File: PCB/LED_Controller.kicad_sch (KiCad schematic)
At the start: 44 parts, among them J1 Conn_01x04_Female, J2 Conn_01x06_Female, J3 Conn_01x06_Female, J4 Add. LED Strip, J5 Add. LED Strip, J7 Conn_01x02, Q1 MMBF170, Q10 BC817, Q2 MMBF170, Q3 MMBF170, Q4 MMBF170, Q9 BC817, SW1 SW_Push, SW2 SW_Push, U1 ESP32-WROOM-32, U2 NCP1117-5.0_SOT223, U3 NCP1117-3.3_SOT223

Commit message: Rev 2.0 local push
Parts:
- removed J1: Conn_01x04_Female, Connector_PinHeader_2.54mm:PinHeader_2x02_P2.54mm_Vertical, symbol Connector:Conn_01x04_Female
- removed J3: Conn_01x06_Female, Connector_PinHeader_2.54mm:PinHeader_2x03_P2.54mm_Vertical, symbol Connector:Conn_01x06_Female
- removed J5: Add. LED Strip, TerminalBlock_Phoenix:TerminalBlock_Phoenix_MKDS-1,5-4-5.08_1x04_P5.08mm_Horizontal, symbol Connector_Generic:Conn_01x04
- removed JP3: Jumper_2_Bridged, Jumper:SolderJumper-2_P1.3mm_Bridged2Bar_Pad1.0x1.5mm, symbol Jumper:Jumper_2_Bridged
- removed JP4: Jumper_3_Bridged12, Jumper:SolderJumper-3_P1.3mm_Bridged2Bar12_Pad1.0x1.5mm, symbol Jumper:Jumper_3_Bridged12
- removed Q1, Q2, Q3, Q4: MMBF170, Package_TO_SOT_SMD:SOT-23, symbol Transistor_FET:MMBF170
- removed Q10, Q9: BC817, Package_TO_SOT_SMD:SOT-23, symbol Transistor_BJT:BC817
- removed R10, R11, R12, R13, R19, R20, R5, R6, R8, R9: 10k, Resistor_SMD:R_0805_2012Metric_Pad1.20x1.40mm_HandSolder, symbol Device:R
- removed SW1, SW2: SW_Push, Button_Switch_SMD:SW_Push_1P1T_NO_CK_KMR2, symbol Switch:SW_Push
- removed U1: ESP32-WROOM-32, RF_Module:ESP32-WROOM-32, symbol RF_Module:ESP32-WROOM-32
- removed U2: NCP1117-5.0_SOT223, Package_TO_SOT_SMD:SOT-223-3_TabPin2, symbol Regulator_Linear:NCP1117-5.0_SOT223
- removed U3: NCP1117-3.3_SOT223, Package_TO_SOT_SMD:SOT-223-3_TabPin2, symbol Regulator_Linear:NCP1117-3.3_SOT223
- added AE1: Antenna_Chip, RF_Antenna:Johanson_2450AT43F0100, symbol Device:Antenna_Chip
- added C10, C11: C, Capacitor_SMD:C_0805_2012Metric_Pad1.18x1.45mm_HandSolder, symbol Device:C
- added C9: 0.1u, Capacitor_SMD:C_0603_1608Metric, symbol Device:C_Small
- added J1: Barrel_Jack, Connector_BarrelJack:BarrelJack_Horizontal, symbol Connector:Barrel_Jack
- added JP1: Jumper_2_Bridged, Jumper:SolderJumper-2_P1.3mm_Bridged2Bar_Pad1.0x1.5mm, symbol Jumper:Jumper_2_Bridged
- added L1: 3.3uH, Inductor_SMD:L_1206_3216Metric_Pad1.22x1.90mm_HandSolder, symbol Device:L
- added L2: L, Inductor_SMD:L_0805_2012Metric_Pad1.05x1.20mm_HandSolder, symbol Device:L
- added U1: ESP32-PICO-D4, Package_DFN_QFN:QFN-48-1EP_7x7mm_P0.5mm_EP5.3x5.3mm, symbol RF_Module:ESP32-PICO-D4
- added U2: AP62200, Package_TO_SOT_SMD:SOT-563, symbol Regulator_Switching:AP62250Z6
- added U3: NCP1117-5.0_SOT223, Package_TO_SOT_SMD:SOT-223-3_TabPin2, symbol Regulator_Linear:NCP1117-5.0_SOT223
- added U4: 74LVCH2T45DC, Package_SO:VSSOP-8_2.3x2mm_P0.5mm, symbol Logic_LevelTranslator:74LVCH2T45DC
- C1: value 10uF -> 0.1uF
- C2: value 0.1uF -> 22uF; footprint Capacitor_SMD:C_0805_2012Metric_Pad1.18x1.45mm_HandSolder -> Capacitor_SMD:C_1206_3216Metric_Pad1.33x1.80mm_HandSolder
- C5: footprint Capacitor_SMD:C_0805_2012Metric_Pad1.18x1.45mm_HandSolder -> Capacitor_SMD:C_1206_3216Metric_Pad1.33x1.80mm_HandSolder
- R4: value 10k -> 31.6k
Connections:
- net PROG_DTR is gone; now on net EN: J2.4 (Pin_4)
- net PROG_RTS is gone; now on net GPIO0: J2.5 (Pin_5)
- net VLED is gone; now on net VIN: C7.1, C8.1, J4.4 (Pin_4)
- net +3V3: now also C2.1, R4.2, C9.1, L1.2, U1.1 (VDDA), U1.19 (VDD3P3_RTC), U1.26 (VDD_SDIO), U1.3 (VDDA3P3), U1.37 (VDD3P3_CPU), U1.4 (VDDA3P3), U1.43 (VDDA), U1.46 (VDDA), U4.1 (VCCA), U4.5 (DIR); no longer R1.1
- net +5V: now also JP1.2 (B), U3.2 (VO), U4.8 (VCCB); no longer C1.1, C2.1, R4.1
- net EN: now also U1.9 (EN)
- net GND: now also R1.1, C10.2, C11.2, C9.2, J1.2, U1.49 (GND), U2.3 (GND), U3.1 (GND), U4.4 (GND); no longer C1.2
- net GPIO0: now also U1.23 (IO0)
- net LED1-CLK_{H}: now also U4.6 (2B)
- net LED1-CLK_{L}: now also U1.16 (IO27), U4.3 (2A)
- net LED1-DATA_{H}: now also U4.7 (1B); no longer R4.2
- net LED1-DATA_{L}: now also U1.17 (IO14), U4.2 (1A); no longer R1.2
- net MIC_SCK: now also U1.13 (IO33)
- net MIC_SD: now also U1.11 (IO35)
- net MIC_WS: now also U1.10 (IO34)
- net RX: now also U1.40 (U0RXD/IO3)
- net TX: now also R7.1, U1.41 (U0TXD/IO1); no longer J2.2 (Pin_2), R7.2
- net VIN: now also J1.1, JP1.1 (A), U2.1 (VIN), U2.5 (EN), U3.3 (VI)
- new net: C1.2, L1.1, U2.2 (SW)
- new net: AE1.1 (FEED), C11.1, L2.2
- new net: J2.2 (Pin_2), R7.2
- new net: R1.2, R4.1, U2.6 (FB)
- new net: C10.1, L2.1, U1.2 (LNA_IN)
- new net: C1.1, U2.4 (BST)
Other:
- moved on the sheet: C3, C4, C5, C6, C7, C8, J2, J7, R7

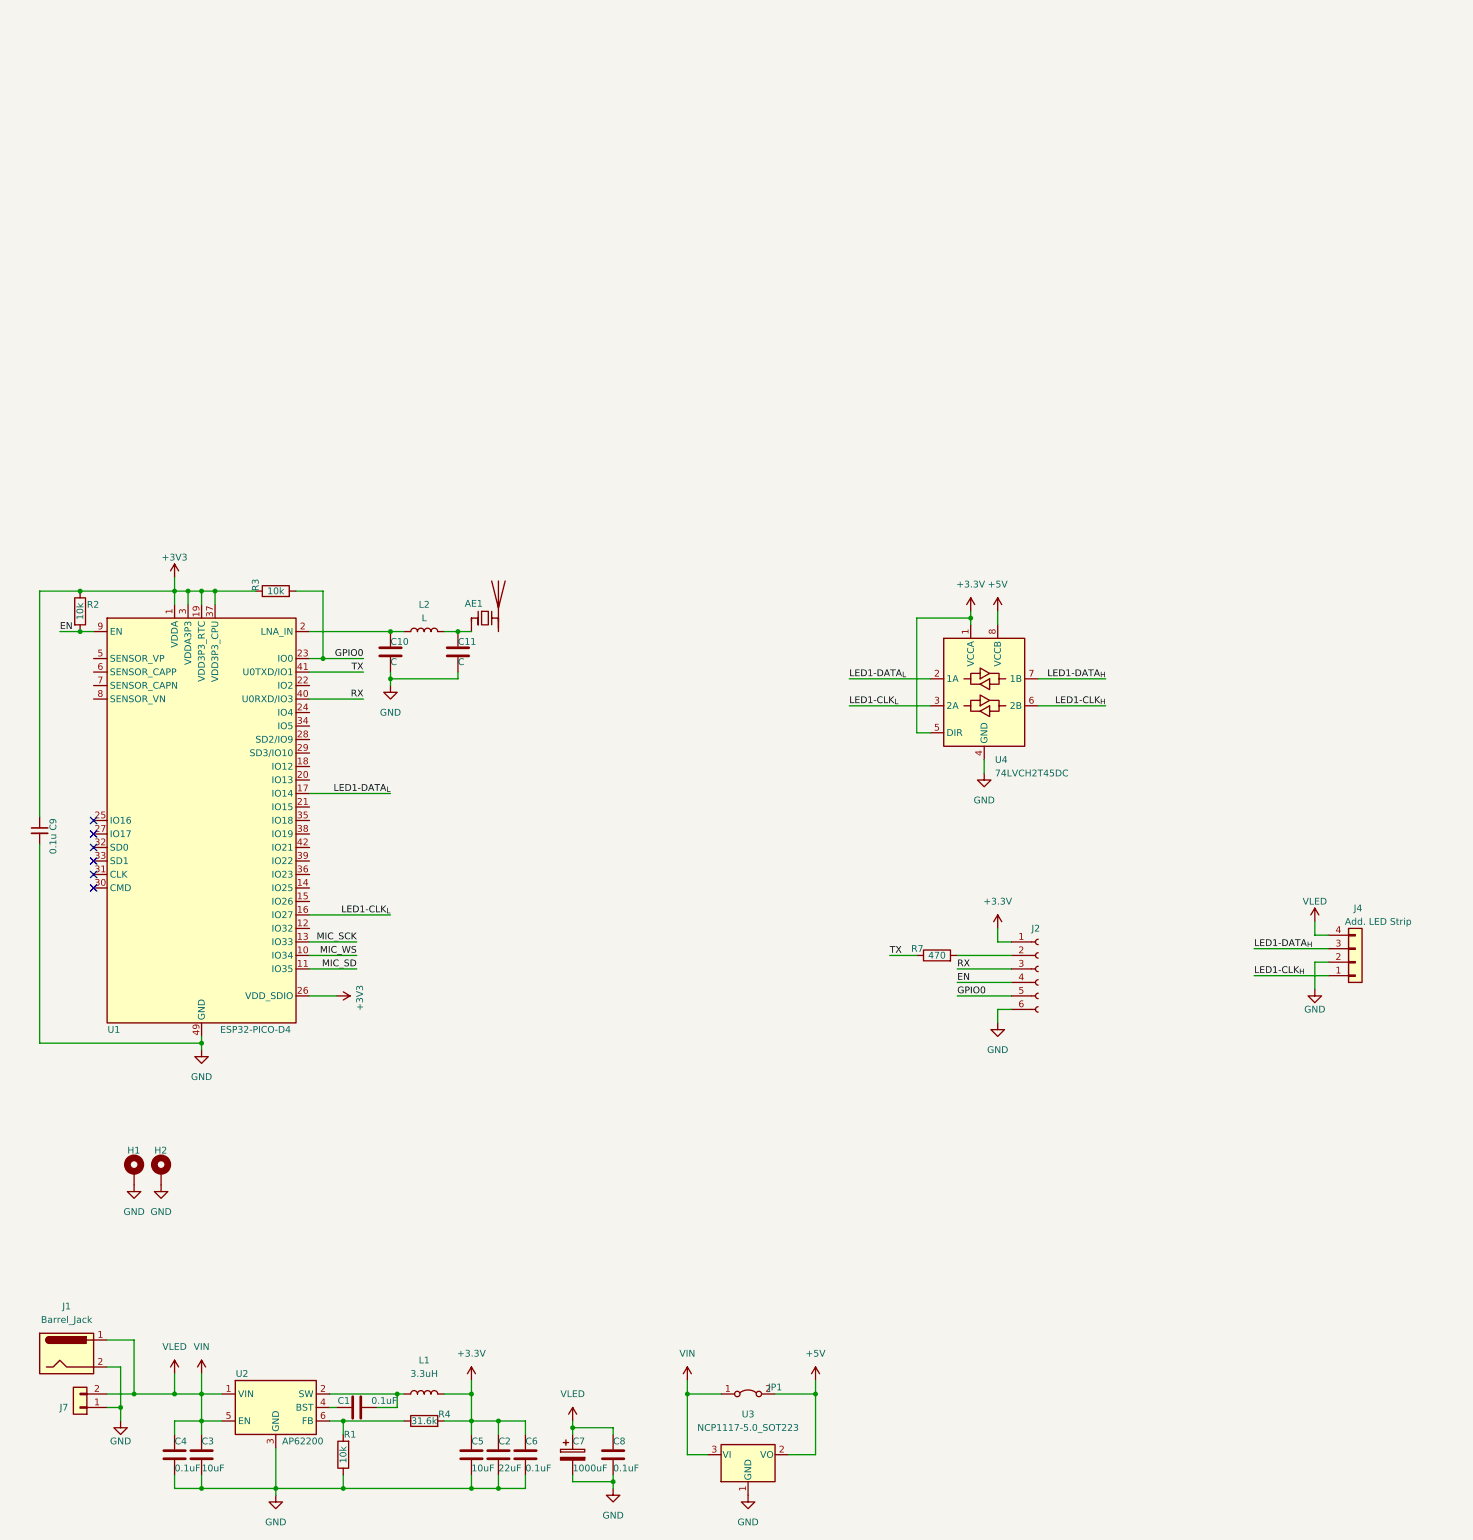
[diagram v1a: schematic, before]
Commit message: Updated README to include impedance matching calculation Updated case for screw tollerance Updated schematic to fill in values for PI network
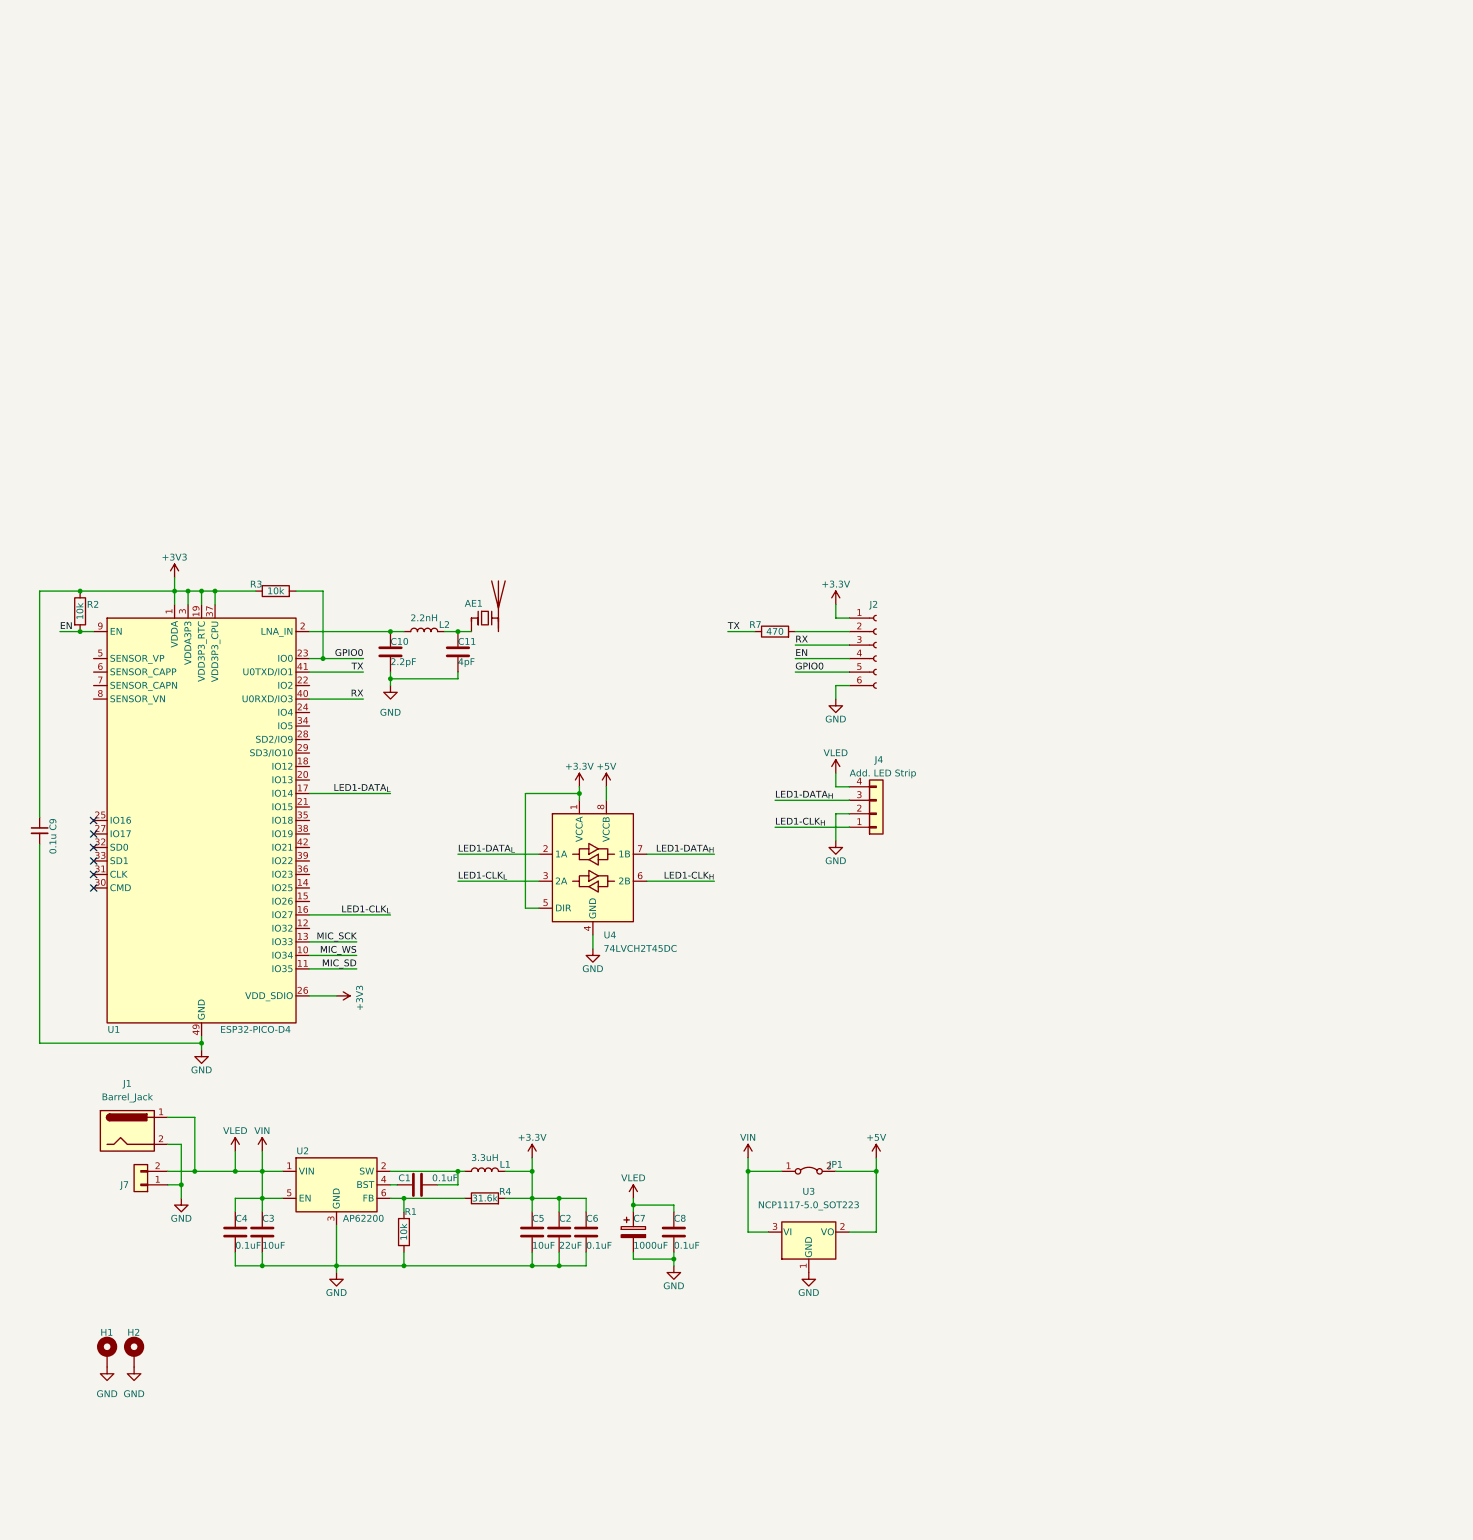
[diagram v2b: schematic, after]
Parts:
- C10: value C -> 2.2pF
- C11: value C -> 4pF
- L2: value L -> 2.2nH
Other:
- title: (none) -> Addressable LED Controller
- moved on the sheet: C1, C2, C3, C4, C5, C6, C7, C8, H1, H2, J1, J2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

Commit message: Started work on V3 of PCB
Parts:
- removed U3: NCP1117-5.0_SOT223, Package_TO_SOT_SMD:SOT-223-3_TabPin2, symbol Regulator_Linear:NCP1117-5.0_SOT223
- added C12, C13, C14, C15: 1uF, symbol Device:C
- added D1: SMF15A, Diode_SMD:D_SMF, symbol Diode:SMF15A
- added F1: Polyfuse, symbol Device:Polyfuse
- added L3, L4: L_Ferrite, symbol Device:L_Ferrite
- added U5: LAN8720A, Package_DFN_QFN:VQFN-24-1EP_4x4mm_P0.5mm_EP2.5x2.5mm_ThermalVias, symbol Interface_Ethernet:LAN8720A
- added U6: MCP1792x-5002xCB, Package_TO_SOT_SMD:SOT-23, symbol Regulator_Linear:MCP1792x-5002xCB
- added Y1: Crystal_GND23, symbol Device:Crystal_GND23
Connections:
- net +3V3: now also L4.2
- net +5V: now also U6.2 (VO)
- net GND: now also C12.2, C13.2, C14.2, C15.2, D1.2 (A2), U5.25 (VSS), U6.1 (GND)
- net VIN: now also U6.3 (VI); no longer C3.1, C4.1, C7.1, C8.1, J1.1, J4.4 (Pin_4), J7.2 (Pin_2), U2.1 (VIN), U2.5 (EN)
- new net: C13.1, C14.1, C15.1, L4.1, U5.1 (VDD2A), U5.19 (VDD1A), U5.9 (VDDIO)
- new net: F1.1, J1.1, J7.2 (Pin_2)
- new net: D1.1 (A1), F1.2, L3.1
- new net: C12.1, U5.6 (VDDCR)
- new net E_CRS: U5.11 (CRS_DV/MODE2)
- new net E_MDC: U5.13 (MDC)
- new net E_MDIO: U5.12 (MDIO)
- new net E_RXD0: U5.8 (RXD0/MODE0)
- new net E_RXD1: U5.7 (RXD1/MODE1)
- new net E_RXER: U5.10 (RXER/PHYAD0)
- new net E_TXD0: U5.17 (TXD0)
- new net E_TXD1: U5.18 (TXD1)
- new net E_TXEN: U5.16 (TXEN)
- new net VLED: C3.1, C4.1, C7.1, C8.1, J4.4 (Pin_4), L3.2, U2.1 (VIN), U2.5 (EN)
- no-connect marks 6 -> 7
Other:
- moved on the sheet: J1, J7, JP1, U4
